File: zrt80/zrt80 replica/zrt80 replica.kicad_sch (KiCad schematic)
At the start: 108 parts, among them J1 VIDEO, J2 POWER, J3 KEYBOARD, J4 S2-S3, J5 RS232, J6 CHAR, J7 RAM, Q1 2N2222, Q2 2N5484, Y1 20MHz, Y2 2.4576MHz

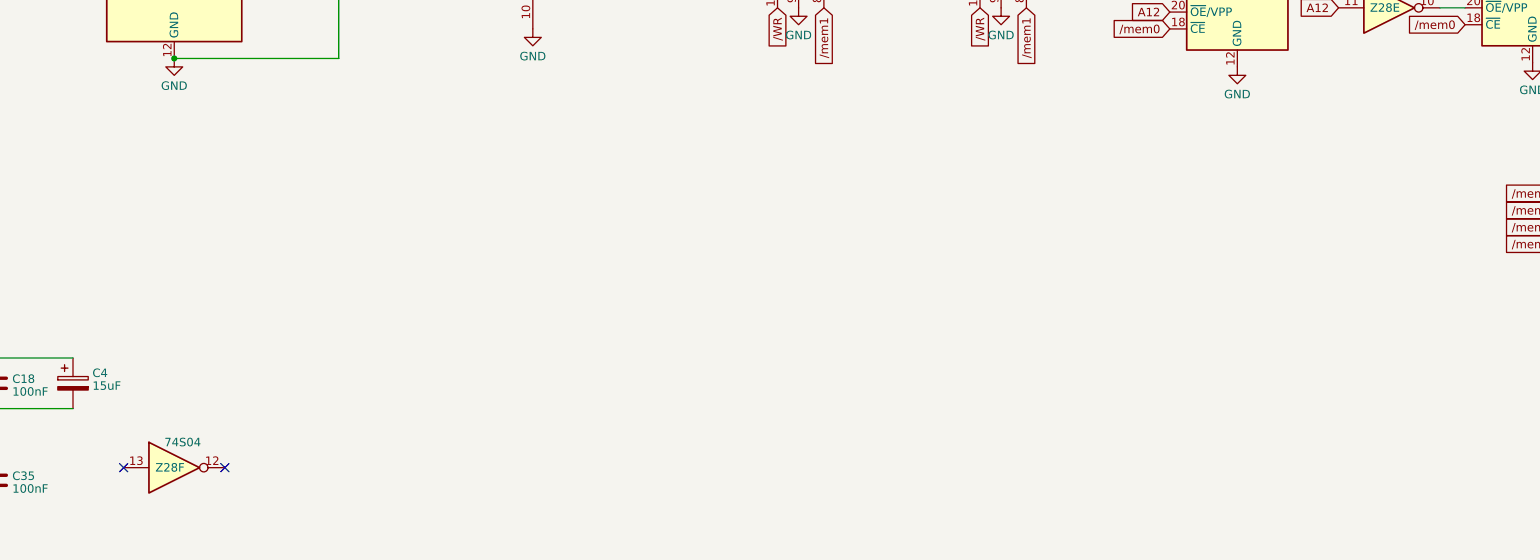
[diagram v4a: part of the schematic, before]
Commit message: updated silk and added note for doubling the rom
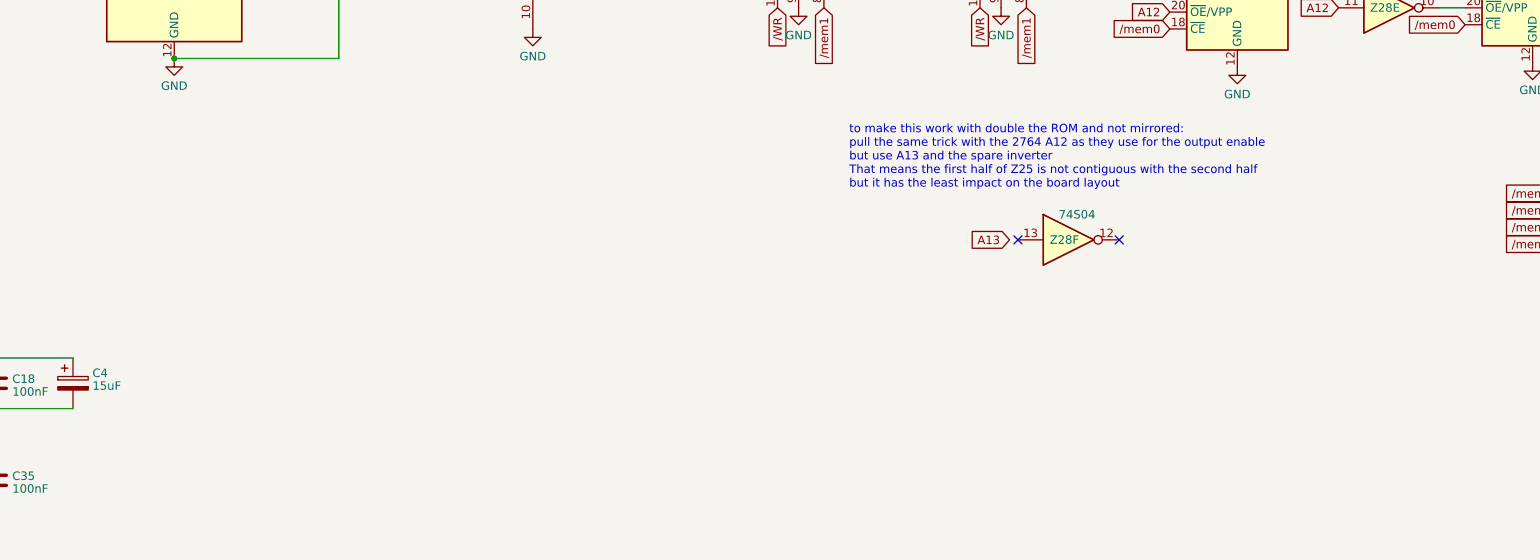
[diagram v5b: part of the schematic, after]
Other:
- note added: "to make this work with double the ROM and not mirrored: pull the same trick with the 2764 A12 as they use for the output enable but use A13 and the spare inverter That means the first half of Z25 is not contiguous with the second half but it has the least impact on the board layout"
- moved on the sheet: Z28F
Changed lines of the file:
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@@
   (no_connect (at 467.995 122.555))
   (no_connect (at 521.97 47.625))
-  (no_connect (at 296.545 397.51))
+  (no_connect (at 431.165 363.22))
   (no_connect (at 534.67 50.165))
   (no_connect (at 493.395 122.555))
@@
   (no_connect (at 451.485 137.16))
   (no_connect (at 534.67 27.305))
-  (no_connect (at 281.305 397.51))
+  (no_connect (at 415.925 363.22))
   (no_connect (at 534.67 55.245))
   (wire (pts (xy 124.46 395.605) (xy 135.89 395.605))
@@
     (stroke (width 0) (type default))
   )
+  (text "to make this work with double the ROM and not mirrored:\npull the same trick with the 2764 A12 as they use for the output enable\nbut use A13 and the spare inverter\nThat means the first half of Z25 is not contiguous with the second half\nbut it has the least impact on the board layout"
+    (at 390.525 355.6 0)
+    (effects (font (size 1.27 1.27)) (justify left bottom))
+  )
   (global_label "D5" (shape input) (at 459.105 308.61 0) (fields_autoplaced)
     (effects (font (size 1.27 1.27)) (justify left))
@@
     )
   )
+  (global_label "A13" (shape input) (at 414.655 363.22 180) (fields_autoplaced)
+    (effects (font (size 1.27 1.27)) (justify right))
+    (property "Intersheetrefs" "${INTERSHEET_REFS}" (at 408.2416 363.22 0)
+      (effects (font (size 1.27 1.27)) (justify right) hide)
+    )
+  )
   (global_label "KBD0" (shape input) (at 278.765 45.085 180) (fields_autoplaced)
     (effects (font (size 1.27 1.27)) (justify right))
@@
     )
   )
-  (symbol (lib_id "74xx:74LS04") (at 288.925 397.51 0) (unit 6)
+  (symbol (lib_id "74xx:74LS04") (at 423.545 363.22 0) (unit 6)
     (in_bom yes) (on_board yes) (dnp no)
-    (property "Reference" "Z28" (at 288.29 397.51 0)
+    (property "Reference" "Z28" (at 422.91 363.22 0)
       (effects (font (size 1.27 1.27)))
     )
-    (property "Value" "74S04" (at 290.195 393.7 0)
+    (property "Value" "74S04" (at 424.815 359.41 0)
       (effects (font (size 1.27 1.27)))
     )
-    (property "Footprint" "Package_DIP:DIP-14_W7.62mm" (at 288.925 397.51 0)
+    (property "Footprint" "Package_DIP:DIP-14_W7.62mm" (at 423.545 363.22 0)
       (effects (font (size 1.27 1.27)) hide)
     )
-    (property "Datasheet" "http://www.ti.com/lit/gpn/sn74LS04" (at 288.925 397.51 0)
+    (property "Datasheet" "http://www.ti.com/lit/gpn/sn74LS04" (at 423.545 363.22 0)
       (effects (font (size 1.27 1.27)) hide)
     )
